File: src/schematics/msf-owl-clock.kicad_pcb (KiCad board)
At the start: 4 copper layers, 129.9 x 183.9 mm, 445 parts, among them Q101 NX6008NBKW, Q301 NX6008NBKW, Q501 NX6008NBKW, Q502 NX6008NBKW, Q503 NX6008NBKW, Q504 NX6008NBKW, Q505 NX6008NBKW, Q601 NX6008NBKW, Q602 BC847BS, Q603 BC847BS, U001 BC805M, U002 TSOP75338TT, U101 MP5016HGQH, U102 BQ24392RSER, U103 FUSB302BMPX, U104 TPS628512DRLR, U201 TPS7A2040PDQNR, U202 TPS7A2036PDBVR, U203 MCP6499, U204 MCP6499, U205 74HC595BQ, U206 TMUX1511RSV, U207 TMUX1511RSV, U301 PIC32CX1025SG41100-I/E5X, U302 AP22653AW6, U401 AP22653AW6, U402 MCP6486U, U403 IS31AP4991A-SLS2, U501 TPS7A2028PDBVR, U502 DPS310XTSA1, U503 HDC3022, U504 VL6180V1NR1, U601 TMUX1574RSV, U602 TMUX1574RSV, U603 TMUX1574RSV

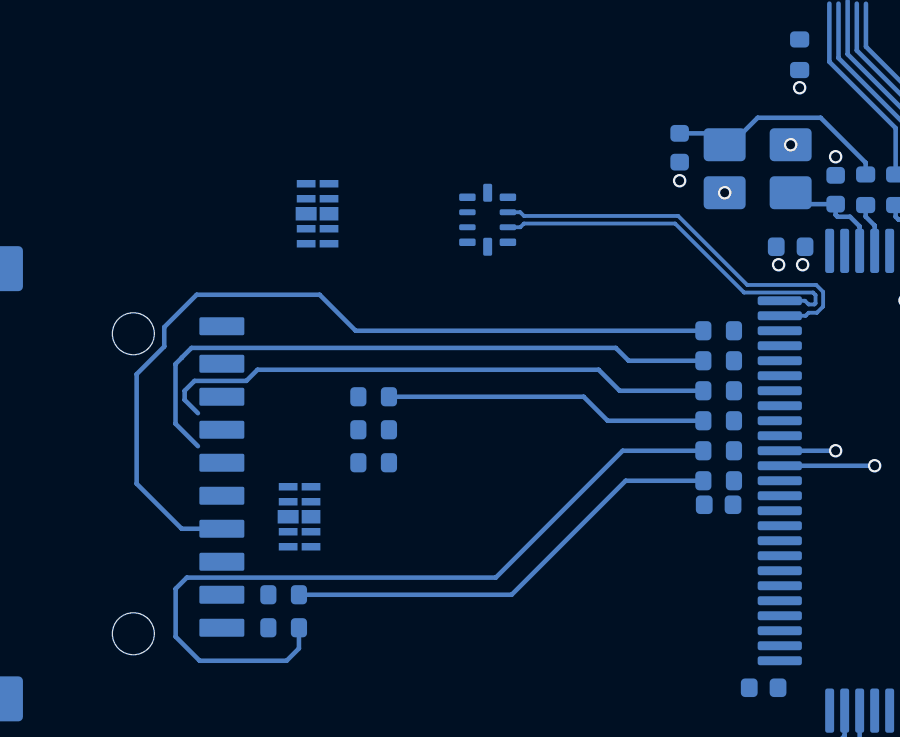
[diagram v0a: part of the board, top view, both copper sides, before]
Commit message: [WIP] Rearranging the SD Card and TVS arrangement.
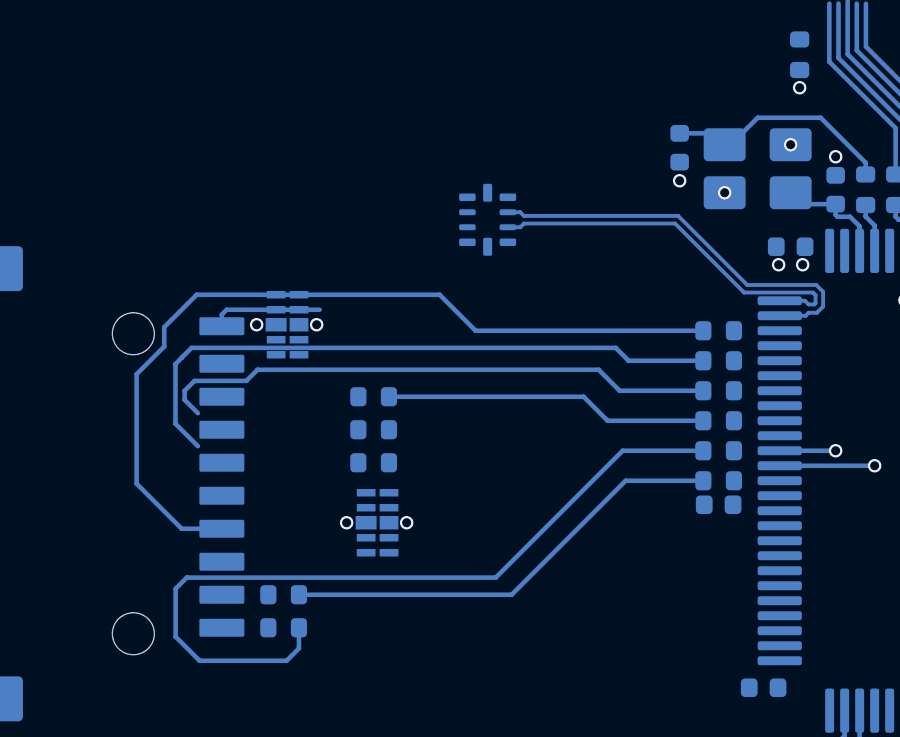
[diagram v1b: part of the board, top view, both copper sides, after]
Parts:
- moved D007 3.83 mm to (54.2, 105.8)
- moved D006 2.61 mm to (57.2, 112.4)
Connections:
- CONN001 pad A6: /D_{+} -> /1-usb-and-power/D+
- CONN001 pad A7: /D_{-} -> /1-usb-and-power/D-
- CONN001 pad B6: /D_{+} -> /1-usb-and-power/D+
- CONN001 pad B7: /D_{-} -> /1-usb-and-power/D-
- D002 pad 4: /D_{-} -> /1-usb-and-power/D-
- D002 pad 5: /D_{+} -> /1-usb-and-power/D+
- D002 pad 6: /D_{+} -> /1-usb-and-power/D+
- D002 pad 7: /D_{-} -> /1-usb-and-power/D-
- D006 pad 1: /3-mcu-core/DAT1 -> /3-mcu-core/DAT0
- D006 pad 10: /3-mcu-core/DAT1 -> /3-mcu-core/DAT0
- D006 pad 2: /3-mcu-core/DAT0 -> /3-mcu-core/DAT1
- D006 pad 4: /3-mcu-core/CLK -> /3-mcu-core/DAT2
- D006 pad 5: /3-mcu-core/CMD -> /3-mcu-core/DAT3
- D006 pad 6: /3-mcu-core/CMD -> /3-mcu-core/DAT3
- D006 pad 7: /3-mcu-core/CLK -> /3-mcu-core/DAT2
- D006 pad 9: /3-mcu-core/DAT0 -> /3-mcu-core/DAT1
- D007 pad 1: /3-mcu-core/DAT3 -> /3-mcu-core/~{WP}
- D007 pad 10: /3-mcu-core/DAT3 -> /3-mcu-core/~{WP}
- D007 pad 2: /3-mcu-core/DAT2 -> /3-mcu-core/CMD
- D007 pad 4: /3-mcu-core/~{WP} -> /3-mcu-core/~{CD}
- D007 pad 5: /3-mcu-core/~{CD} -> /3-mcu-core/CLK
- D007 pad 6: /3-mcu-core/~{CD} -> /3-mcu-core/CLK
- D007 pad 7: /3-mcu-core/~{WP} -> /3-mcu-core/~{CD}
- D007 pad 9: /3-mcu-core/DAT2 -> /3-mcu-core/CMD
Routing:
- net /3-mcu-core/~{CD}: track 3.16 -> 6.88 mm
- net GND: vias 14 -> 18

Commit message: Rearranged the SD Card and TVS placements.
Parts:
- removed NT301, NT302: Net Tie, restall-generic-wires:net-tie-2-6mil
- removed the R332 at (319.8, 103.8)
- removed the R333 at (319.8, 105.8)
- removed the R334 at (319.8, 107.8)
- removed the R335 at (319.8, 109.8)
- removed the R336 at (319.8, 111.8)
- added R018: 43Ω, restall-generic-resistors:nominal-0402-1005, B.Cu at (105.1, 95.9)
- added R019: 43Ω, restall-generic-resistors:nominal-0402-1005, B.Cu at (106.2, 95.9)
- added R020: 43Ω, restall-generic-resistors:nominal-0402-1005, B.Cu at (110.6, 95.9)
- added R021: 43Ω, restall-generic-resistors:nominal-0402-1005, B.Cu at (111.7, 95.9)
- added R022: 43Ω, restall-generic-resistors:nominal-0402-1005, B.Cu at (112.8, 95.9)
- C336: moved to B.Cu
- R327, R328: value 43Ω -> 33kΩ
- R329, R330: value 43Ω -> 330Ω; moved to F.Cu
- R331: moved to F.Cu
- moved C336 192.9 mm to (109.5, 95.9), turned to -90 degrees
- moved R331 132.4 mm to (186.4, 118.6), turned to 0 degrees
- moved R330 132.3 mm to (186.3, 120.6), turned to 0 degrees
- moved R329 130.0 mm to (186.3, 122.4), turned to 0 degrees
- moved CONN002 67.5 mm to (109.9, 88.1), turned to 0 degrees
- moved D007 61.8 mm to (115.2, 95.9), turned to 0 degrees
- moved R328 59.5 mm to (115.6, 98.2), turned to 90 degrees
- moved R327 58.4 mm to (114.2, 98.2), turned to 90 degrees
- moved U102 57.8 mm to (118.7, 102.6), turned to 90 degrees
- moved D006 56.3 mm to (111.7, 98.2), turned to 0 degrees
- moved R306 55.3 mm to (124.2, 113.0), turned to 0 degrees
- moved C318 54.6 mm to (121.1, 109.0), turned to 180 degrees
- moved C308 54.3 mm to (125.3, 117.1), turned to 0 degrees
- moved L301 52.7 mm to (125.3, 120.6), turned to 90 degrees
- moved XTAL302 51.7 mm to (120.4, 111.6), turned to 90 degrees
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- renumbered R337 to R332, R338 to R333, R339 to R334, R340 to R335, R341 to R336, R342 to R337, R343 to R338, R344 to R339, R345 to R340, R346 to R341, R347 to R342, R348 to R343, R349 to R344, R350 to R345, R351 to R346, R352 to R347
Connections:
- CONN002 pad 1: /3-mcu-core/DAT2 -> Net-(CONN002-DAT2)
- CONN002 pad 2: /3-mcu-core/DAT3 -> Net-(CONN002-DAT3/CD)
- CONN002 pad 3: /3-mcu-core/CMD -> Net-(CONN002-CMD)
- CONN002 pad 6: Net-(CONN002-VSS) -> GND
- CONN002 pad 7: /3-mcu-core/DAT0 -> Net-(CONN002-DAT0)
- CONN002 pad 8: /3-mcu-core/DAT1 -> Net-(CONN002-DAT1)
- R322 pad 2: Net-(R322-Pad2) -> /3-mcu-core/CMD
- R323 pad 2: Net-(R323-Pad2) -> /3-mcu-core/DAT3
- R324 pad 2: Net-(R324-Pad2) -> /3-mcu-core/DAT2
- R325 pad 2: Net-(R325-Pad2) -> /3-mcu-core/DAT1
- R326 pad 2: Net-(R326-Pad2) -> /3-mcu-core/DAT0
- R327 pad 1: Net-(R322-Pad2) -> /1-usb-and-power/~{USB_SUSPEND}
- R327 pad 2: /3-mcu-core/CMD -> /3-mcu-core/~{WP}
- R328 pad 1: Net-(R323-Pad2) -> /1-usb-and-power/~{USB_SUSPEND}
- R328 pad 2: /3-mcu-core/DAT3 -> /3-mcu-core/~{CD}
- R329 pad 1: Net-(R324-Pad2) -> Net-(U301-PC21)
- R329 pad 2: /3-mcu-core/DAT2 -> /3-mcu-core/BC805M.SWDIO
- R330 pad 1: Net-(R325-Pad2) -> Net-(U301-PC20)
- R330 pad 2: /3-mcu-core/DAT1 -> /3-mcu-core/BC805M.SWDCLK
- R331 pad 1: Net-(R326-Pad2) -> Net-(U301-PC19)
- R331 pad 2: /3-mcu-core/DAT0 -> /3-mcu-core/BC805M.MOSI
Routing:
- net Net-(R325-Pad2): track 26.4 -> 0.00 mm
- net /3-mcu-core/DAT1: track 0.00 -> 26.1 mm
- net /3-mcu-core/CMD: track 0.00 -> 24.6 mm
- net /3-mcu-core/DAT3: track 0.00 -> 22.3 mm
- net Net-(R322-Pad2): track 21.0 -> 0.00 mm
- net Net-(R323-Pad2): track 18.8 -> 0.00 mm
- net /3-mcu-core/DAT0: track 0.00 -> 17.5 mm
- net Net-(R326-Pad2): track 15.1 -> 0.00 mm
- net /3-mcu-core/DAT2: track 0.00 -> 13.6 mm
- net Net-(R324-Pad2): track 10.8 -> 0.00 mm
- net /3-mcu-core/~{WP}: track 1.86 -> 5.94 mm
- net Net-(U301-PB18): track 0.00 -> 2.36 mm
- net /1-usb-and-power/SDA: track 0.00 -> 2.27 mm, vias 0 -> 1
- net Net-(U301-PA21): track 0.00 -> 2.26 mm
- net /1-usb-and-power/SCL: track 0.00 -> 2.16 mm, vias 0 -> 1
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
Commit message: Started laying out the USB lines.
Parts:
- C111, C112, C113, C114, C115, CONN001, D002, R107, R108, R336, R337, R338, R339, R340, R341, R342, U103: moved to B.Cu
- moved U103 234.1 mm to (147.2, 113.4), turned to -90 degrees
- moved R108 233.9 mm to (140.7, 115.6), turned to 90 degrees
- moved R107 232.9 mm to (141.7, 115.6), turned to 90 degrees
- moved C112 230.4 mm to (144.5, 113.4), turned to 180 degrees
- moved C114 230.3 mm to (144.5, 114.8), turned to 180 degrees
- moved C115 230.1 mm to (144.5, 112.0), turned to 180 degrees
- moved CONN001 228.8 mm to (141.9, 122.0)
- moved C111 227.7 mm to (147.2, 110.7), turned to 90 degrees
- moved C113 226.5 mm to (148.2, 110.7), turned to 90 degrees
- moved R336 220.9 mm to (102.2, 90.3), turned to -90 degrees
- moved R337 220.0 mm to (103.2, 90.3), turned to -90 degrees
- moved R338 219.2 mm to (104.2, 90.3), turned to -90 degrees
- moved R339 218.4 mm to (105.2, 90.3), turned to -90 degrees
- moved R341 217.5 mm to (108.2, 90.3), turned to -90 degrees
- moved R340 216.6 mm to (107.2, 90.3), turned to -90 degrees
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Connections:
- D002 pad 1: /1-usb-and-power/CC1 -> /1-usb-and-power/D-
- D002 pad 10: /1-usb-and-power/CC1 -> /1-usb-and-power/D-
- D002 pad 2: /1-usb-and-power/CC2 -> /1-usb-and-power/D+
- D002 pad 4: /1-usb-and-power/D- -> /1-usb-and-power/CC2
- D002 pad 5: /1-usb-and-power/D+ -> /1-usb-and-power/CC1
- D002 pad 6: /1-usb-and-power/D+ -> /1-usb-and-power/CC1
- D002 pad 7: /1-usb-and-power/D- -> /1-usb-and-power/CC2
- D002 pad 9: /1-usb-and-power/CC2 -> /1-usb-and-power/D+
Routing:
- net /1-usb-and-power/CC2: track 0.00 -> 15.1 mm
- net /1-usb-and-power/D-: track 0.00 -> 14.1 mm
- net /1-usb-and-power/D+: track 0.00 -> 13.3 mm
- net /1-usb-and-power/CC1: track 0.00 -> 7.90 mm, vias 0 -> 2
- net Net-(U301-PA08): track 0.00 -> 2.75 mm
- net Net-(U301-PA09): track 0.00 -> 2.36 mm
- net Net-(U301-PA10): track 0.00 -> 1.91 mm
- net Net-(U301-PA11): track 0.00 -> 1.65 mm
- net Net-(U301-PB10): track 0.00 -> 1.61 mm
- net Net-(U102-DP_CON): track 0.00 -> 1.27 mm
- net Net-(U102-DM_CON): track 0.00 -> 1.27 mm
- net Net-(NT005-P1_PASSIVE): vias 0 -> 1
- net GND: vias 37 -> 53
- net /CORE_VDD_{+3.3V}: vias 0 -> 6
- net /3-mcu-core/MCU_AV_{DD}: vias 3 -> 2
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
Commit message: Simplified the owl PCB outline, made it more symmetrical, and closed the shape correctly so that it acts as a proper board edge.
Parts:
- removed NT002: Net Tie, restall-generic-wires:net-tie-2-6mil
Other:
- board size 129.9 x 183.9 mm -> 130.1 x 183.6 mm

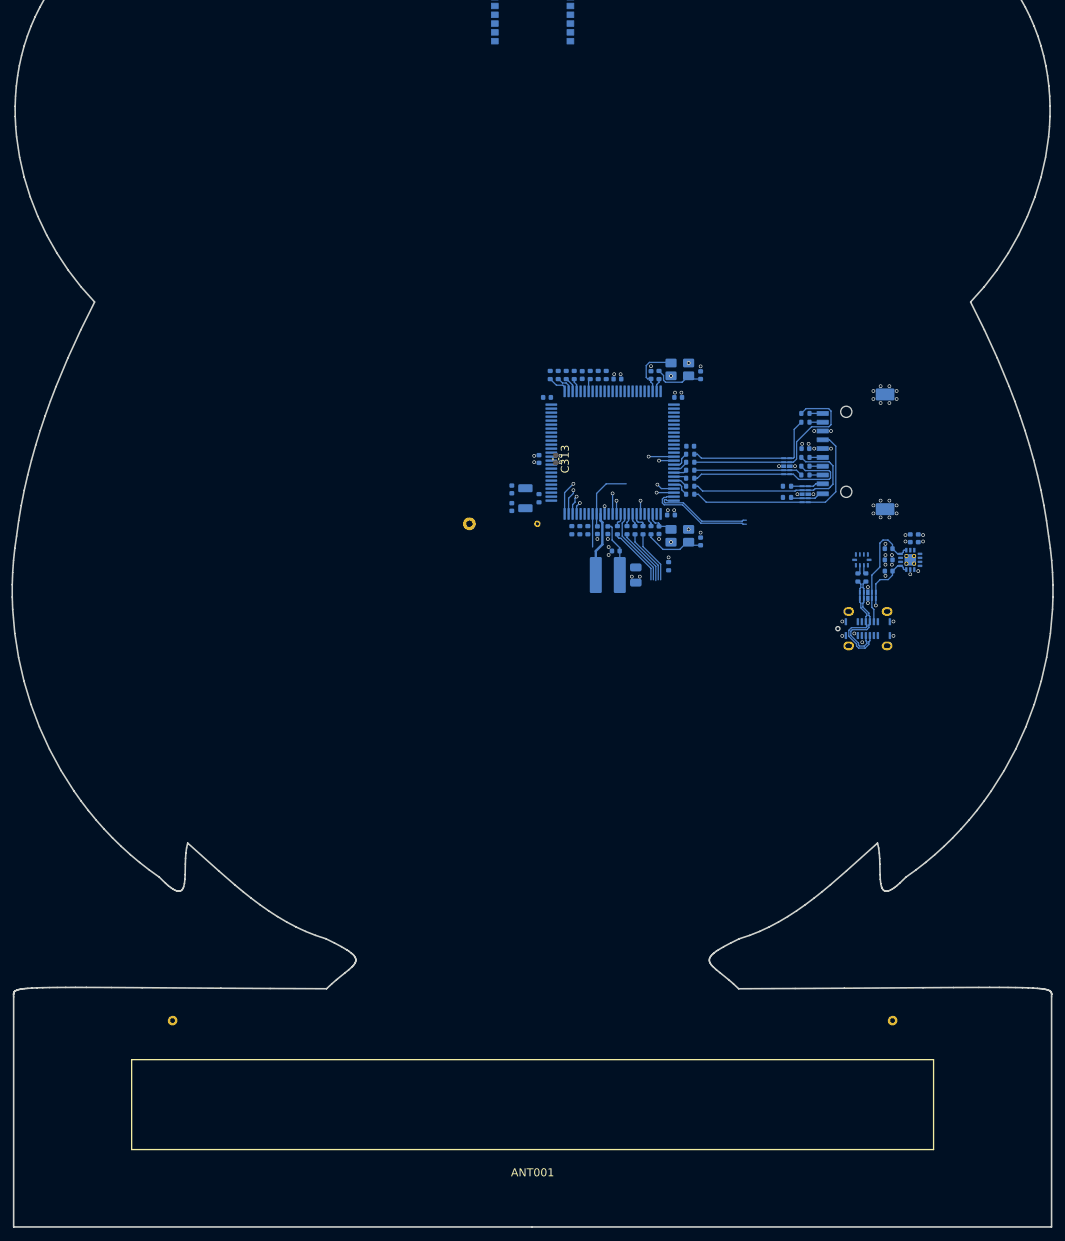
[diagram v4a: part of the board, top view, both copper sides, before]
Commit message: Added tooling holes for JLCPCB's PCBA.
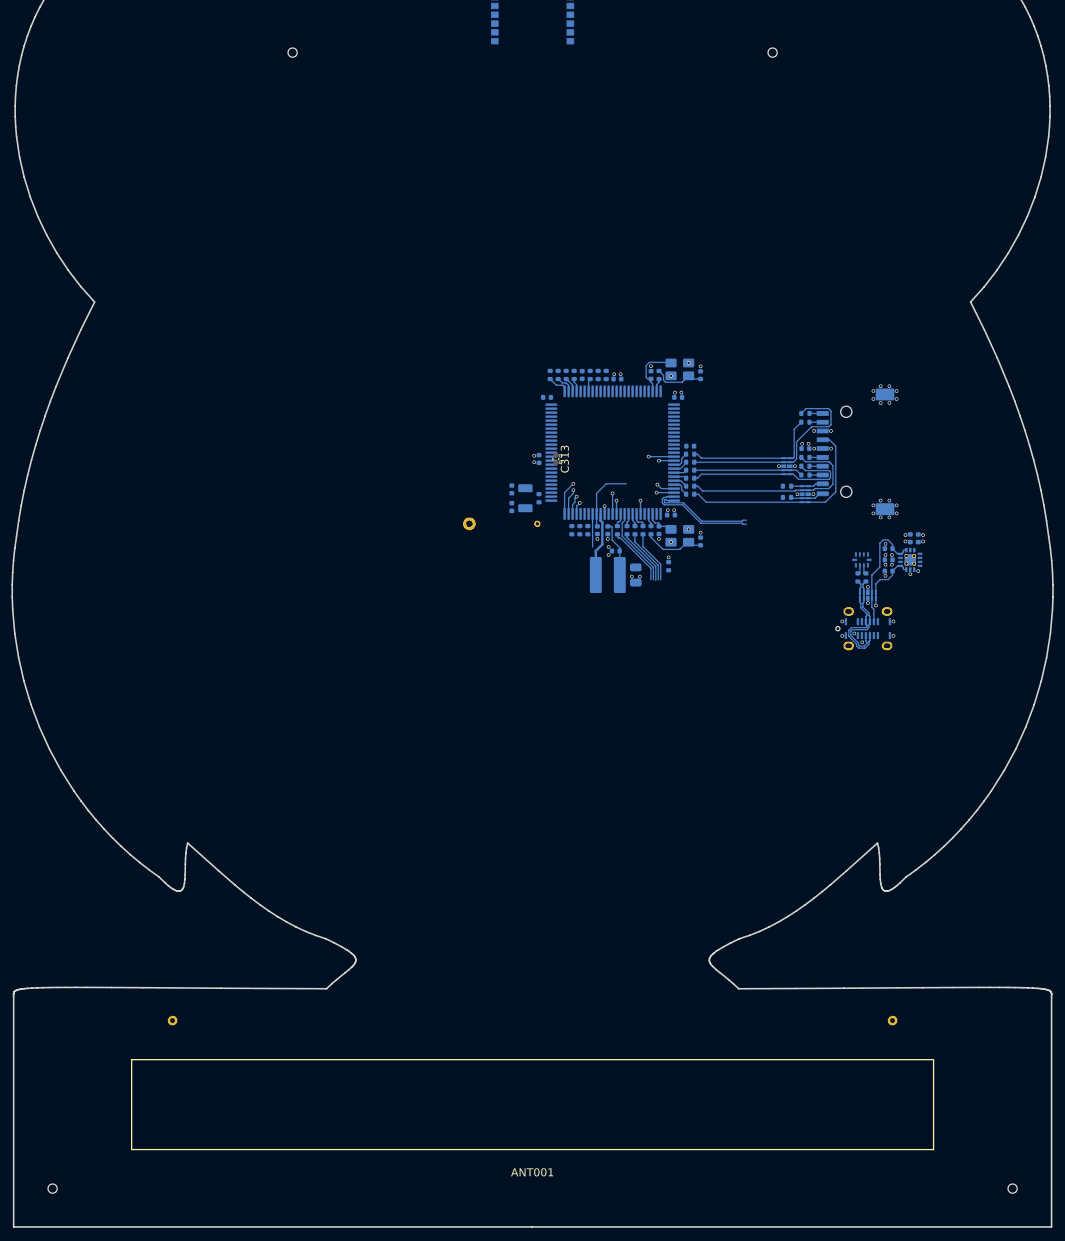
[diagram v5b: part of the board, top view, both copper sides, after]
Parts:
- added REF**: tooling-hole, restall-manufacturer-jlcpcb:tooling-hole, F.Cu at (160.0, 192.0)
- added REF**: tooling-hole, restall-manufacturer-jlcpcb:tooling-hole, F.Cu at (40.0, 192.0)
- added REF**: tooling-hole, restall-manufacturer-jlcpcb:tooling-hole, F.Cu at (70.0, 50.0)
- added REF**: tooling-hole, restall-manufacturer-jlcpcb:tooling-hole, F.Cu at (130.0, 50.0)
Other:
- board text added: "Tooling Holes: https://jlcpcb.com/help/article/47-How-to-add-tooling-holes-for-PCB-assembly-order"
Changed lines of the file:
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@@
     )
   )
+  (footprint "restall-manufacturer-jlcpcb:tooling-hole" (layer "F.Cu")
+    (at 160 192)
+    (descr "Tooling Hole for PCBA")
+    (tags "pcba tooling hole fiducial jlcpcb")
+    (solder_mask_margin 0.148)
+    (clearance 0.248)
+    (attr through_hole board_only exclude_from_bom allow_missing_courtyard)
+    (fp_text reference "REF**" (at 0 -0.5 unlocked) (layer "F.SilkS") hide
+        (effects (font (size 1 1) (thickness 0.15)))
+    )
+    (fp_text value "tooling-hole" (at 0 1 unlocked) (layer "F.Fab")
+        (effects (font (size 1 1) (thickness 0.15)))
+    )
+    (pad "" np_thru_hole circle (at 0 0) (size 1.152 1.152) (drill 1.152) (layers "F&B.Cu" "*.Mask")
+      (solder_mask_margin 0.148) (clearance 0.248) (zone_connect 0))
+  )
   (footprint "restall-generic-capacitors:unpolarised-nominal-0603-1608" (layer "F.Cu")
     (at 409.62 106.76)
@@
     )
   )
+  (footprint "restall-manufacturer-jlcpcb:tooling-hole" (layer "F.Cu")
+    (at 40 192)
+    (descr "Tooling Hole for PCBA")
+    (tags "pcba tooling hole fiducial jlcpcb")
+    (solder_mask_margin 0.148)
+    (clearance 0.248)
+    (attr through_hole board_only exclude_from_bom allow_missing_courtyard)
+    (fp_text reference "REF**" (at 0 -0.5 unlocked) (layer "F.SilkS") hide
+        (effects (font (size 1 1) (thickness 0.15)))
+    )
+    (fp_text value "tooling-hole" (at 0 1 unlocked) (layer "F.Fab")
+        (effects (font (size 1 1) (thickness 0.15)))
+    )
+    (pad "" np_thru_hole circle (at 0 0) (size 1.152 1.152) (drill 1.152) (layers "F&B.Cu" "*.Mask")
+      (solder_mask_margin 0.148) (clearance 0.248) (zone_connect 0))
+  )
   (footprint "restall-generic-sop:MSOP8-3x3mm-0.65mm" (layer "F.Cu")
     (at 408.24 111.24)
@@
     )
   )
+  (footprint "restall-manufacturer-jlcpcb:tooling-hole" (layer "F.Cu")
+    (at 70 50)
+    (descr "Tooling Hole for PCBA")
+    (tags "pcba tooling hole fiducial jlcpcb")
+    (solder_mask_margin 0.148)
+    (clearance 0.248)
+    (attr through_hole board_only exclude_from_bom allow_missing_courtyard)
+    (fp_text reference "REF**" (at 0 -0.5 unlocked) (layer "F.SilkS") hide
+        (effects (font (size 1 1) (thickness 0.15)))
+    )
+    (fp_text value "tooling-hole" (at 0 1 unlocked) (layer "F.Fab")
+        (effects (font (size 1 1) (thickness 0.15)))
+    )
+    (pad "" np_thru_hole circle (at 0 0) (size 1.152 1.152) (drill 1.152) (layers "F&B.Cu" "*.Mask")
+      (solder_mask_margin 0.148) (clearance 0.248) (zone_connect 0))
+  )
   (footprint "restall-generic-capacitors:unpolarised-nominal-0402-1005" (layer "F.Cu")
     (at 371.64 101.79)
@@
     )
   )
+  (footprint "restall-manufacturer-jlcpcb:tooling-hole" (layer "F.Cu")
+    (at 130 50)
+    (descr "Tooling Hole for PCBA")
+    (tags "pcba tooling hole fiducial jlcpcb")
+    (solder_mask_margin 0.148)
+    (clearance 0.248)
+    (attr through_hole board_only exclude_from_bom allow_missing_courtyard)
+    (fp_text reference "REF**" (at 0 -0.5 unlocked) (layer "F.SilkS") hide
+        (effects (font (size 1 1) (thickness 0.15)))
+    )
+    (fp_text value "tooling-hole" (at 0 1 unlocked) (layer "F.Fab")
+        (effects (font (size 1 1) (thickness 0.15)))
+    )
+    (pad "" np_thru_hole circle (at 0 0) (size 1.152 1.152) (drill 1.152) (layers "F&B.Cu" "*.Mask")
+      (solder_mask_margin 0.148) (clearance 0.248) (zone_connect 0))
+  )
   (footprint "restall-manufacturer-diodes-inc:D5V0FS4U10LP" (layer "F.Cu")
     (at 331.91 76.29)
@@
     (effects (font (size 1 1) (thickness 0.15)))
   )
+  (gr_text "Tooling Holes:\nhttps://jlcpcb.com/help/article/47-How-to-add-tooling-holes-for-PCB-assembly-order" (at 200 20) (layer "F.Fab")
+    (effects (font (size 1 1) (thickness 0.15)) (justify left bottom))
+  )
   (via (at 144.908677 114.008677) (size 0.45) (drill 0.3) (layers "F.Cu" "B.Cu") (remove_unused_layers) (keep_end_layers) (zone_layer_connections) (net 3))
